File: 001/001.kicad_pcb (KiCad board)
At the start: 2 copper layers, 24.5 x 22 mm, 7 parts, among them J1 USB, J2 Conn_01x14

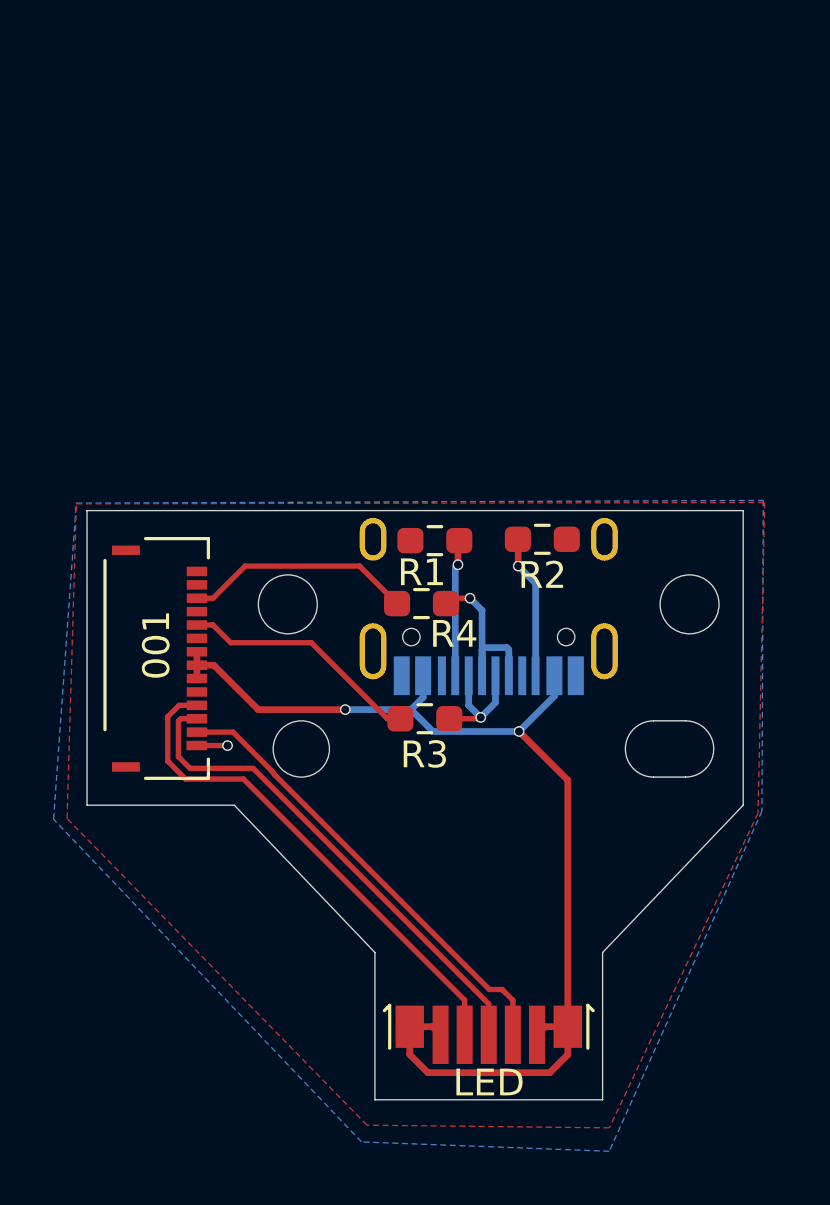
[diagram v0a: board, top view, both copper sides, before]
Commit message: Modified 001 to have pads to be used for 011 as well.
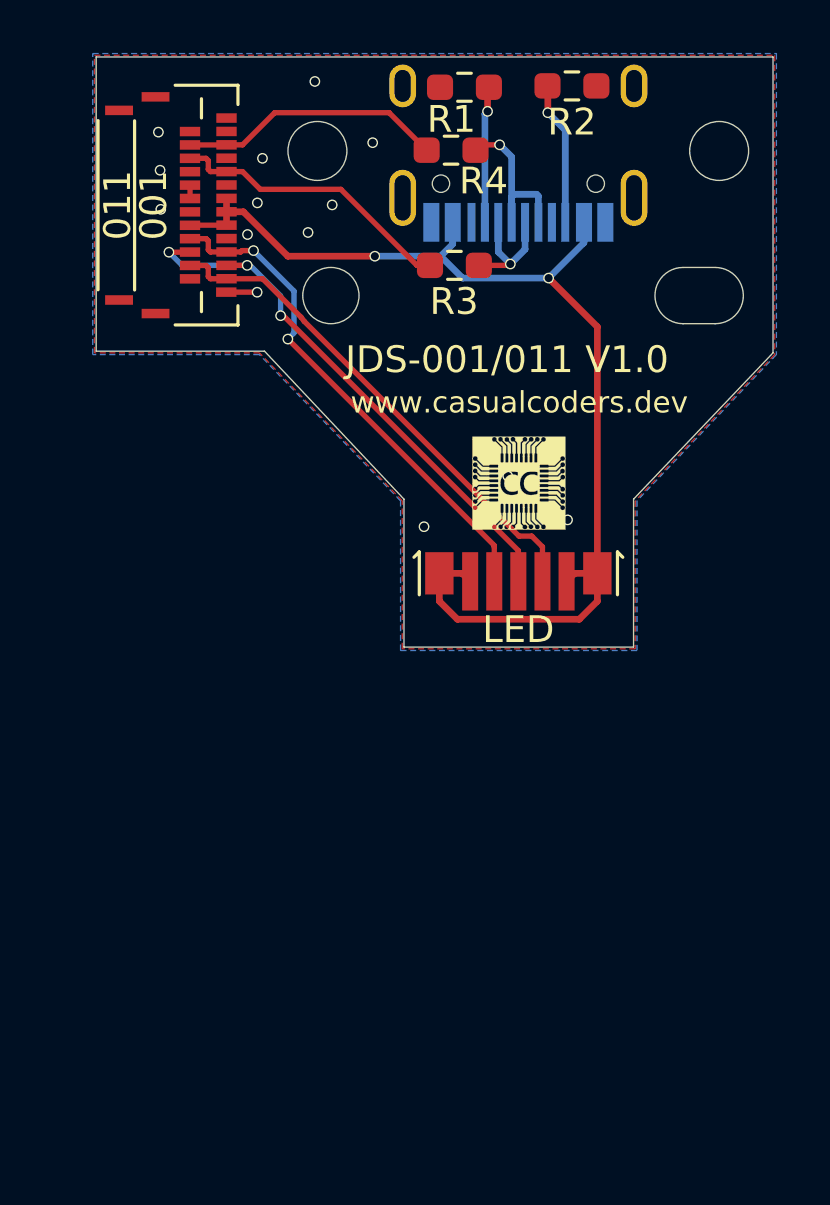
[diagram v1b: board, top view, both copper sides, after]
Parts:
- added 011: Conn_01x12, Molex 5034801200:503480-1200, F.Cu at (106.1, 58.9)
- added G***: LOGO, MSL0104RGB:3.5mm CC_Logo, F.Cu at (119.9, 69.3)
- USB: renamed from J1; value USB -> USB_C_Receptacle_USB2.0
- moved R1 17.0 mm to (117.9, 54.5)
- moved USB 17.0 mm to (119.9, 55.5)
- moved J2 17.0 mm to (107.5, 58.4)
- moved R3 17.0 mm to (117.5, 61.1)
- moved R4 17.0 mm to (117.4, 56.8)
- moved D1 17.0 mm to (119.9, 72.9)
- moved R2 17.0 mm to (121.9, 54.4)
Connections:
- net /vcc renamed VCC
- net Net-(D1-Pad3) renamed /G
- net Net-(D1-Pad4) renamed /R
- net Net-(D1-Pad5) renamed /B
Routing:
- net /R: track 18.6 -> 20.8 mm, vias 0 -> 3
- net /B: track 18.0 -> 19.8 mm
- net /d-: track 9.05 -> 10.8 mm
- net VCC: track 41.0 -> 42.4 mm
- net /d+: track 8.55 -> 9.91 mm
- net Net-(J3-Pad5): track 0.00 -> 0.50 mm
- net /G: track 20.0 -> 20.1 mm, vias 0 -> 2
- net GND: vias 1 -> 14
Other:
- board size 24.5 x 22 mm -> 25.3 x 22 mm
- board text added: "JDS-001/011 V1.0"
- board text added: "www.casualcoders.dev"

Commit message: Added credit to 001/011 boards. Thanks to IcicaSora and Martain Refseth for this board!
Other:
- board text added: "Thanks to Martain Refseth and IcicaSora for the schematic and dimensions"
